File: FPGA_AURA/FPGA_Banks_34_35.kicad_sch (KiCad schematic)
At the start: 1 part, among them U1 XC7A35T-2FTG256C

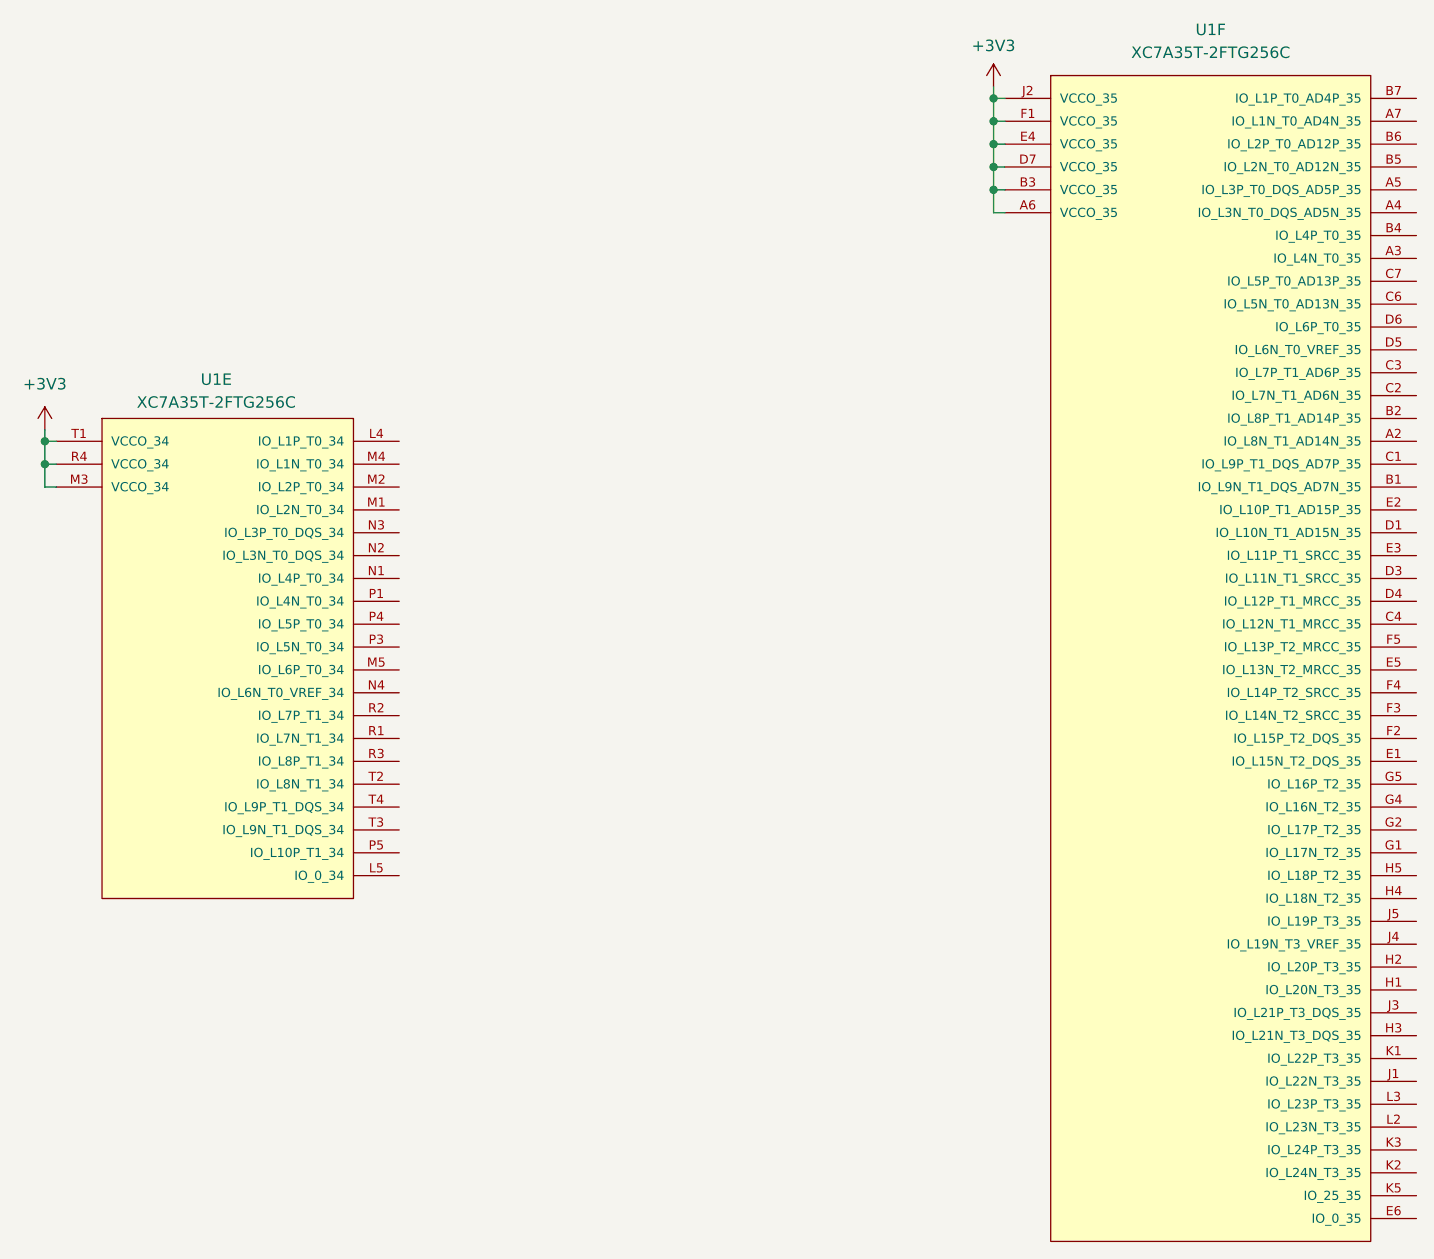
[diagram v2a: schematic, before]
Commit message: Changing stackup to 10 layers and connectors change
Development has been slow due to SI concerns with 8 layers so changing the layer count to 10 will simplify design. The picoblade/SD connector(s) are large and not high speed, so a high speed mezzanine will be used to go to a daughter board with the picoblade connectors and SD card, or other devices/protocols e.g. ADCs, COAX, IMUs, etc.
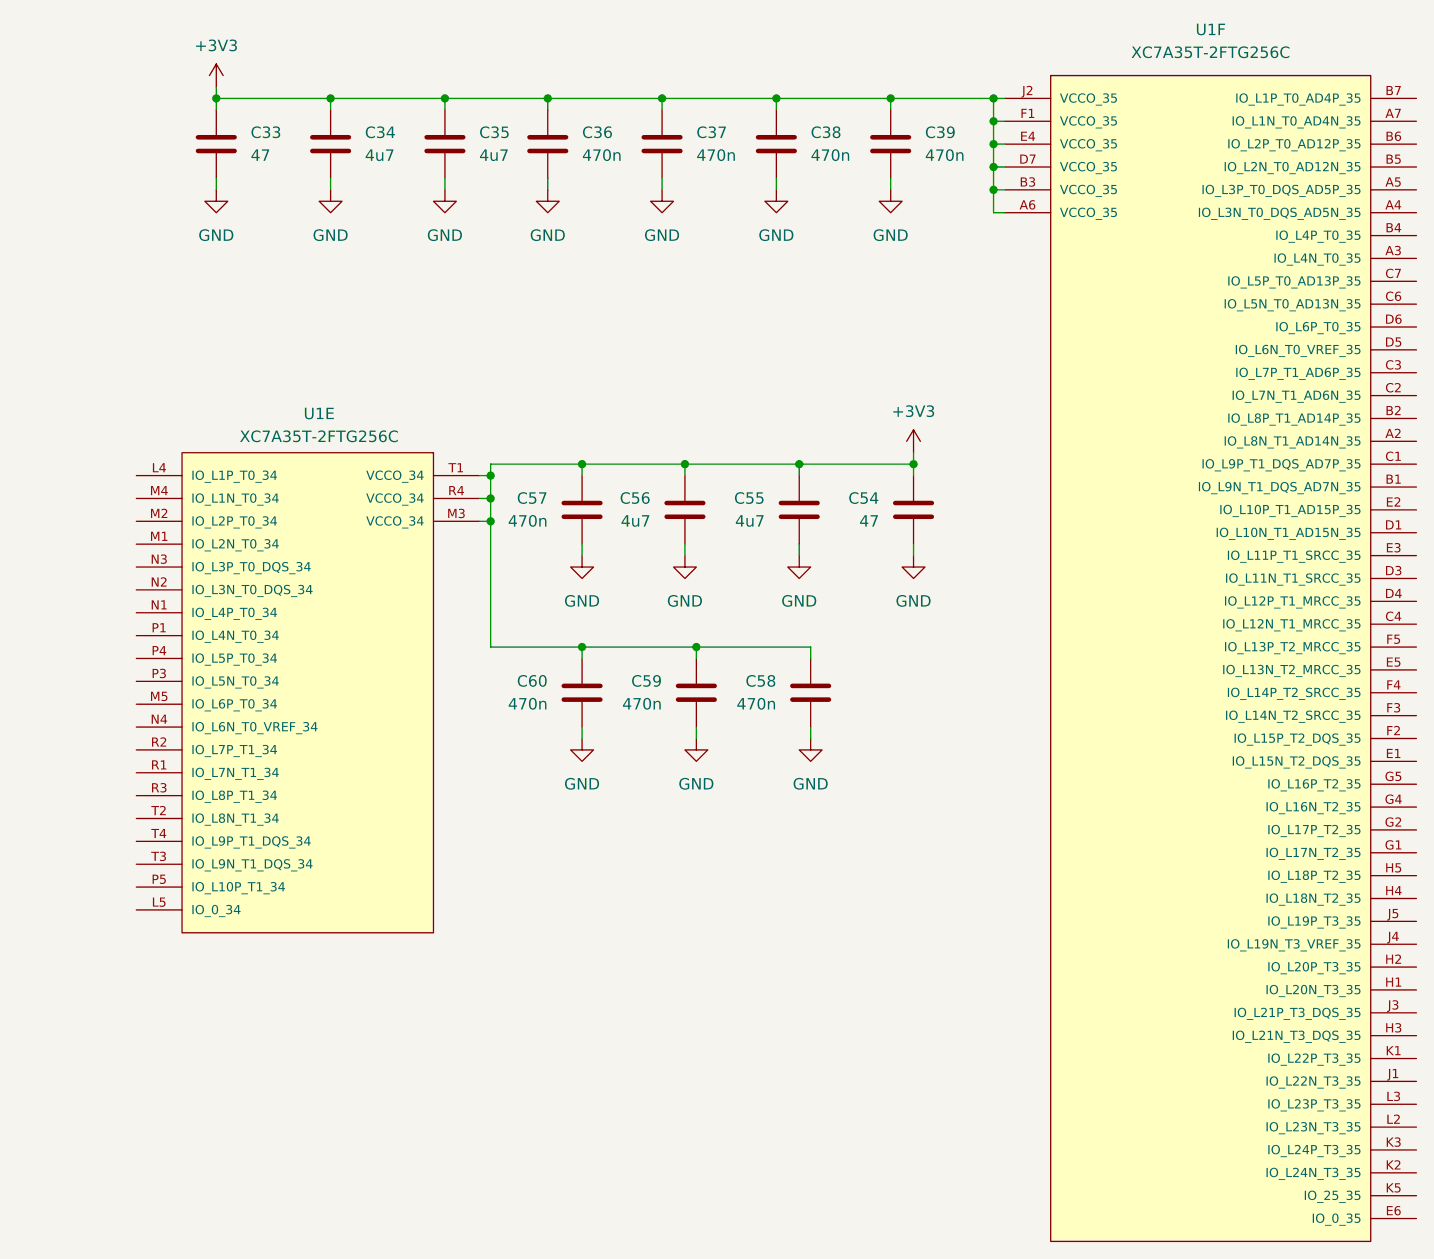
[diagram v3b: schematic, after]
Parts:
- added C33, C54: 47, Capacitor_SMD:C_0603_1608Metric, symbol Device:C
- added C34, C35, C55, C56: 4u7, Capacitor_SMD:C_0603_1608Metric, symbol Device:C
- added C36, C37, C38, C39, C57, C58, C59, C60: 470n, Capacitor_SMD:C_0402_1005Metric, symbol Device:C
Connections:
- net +3V3: now also C33.1, C34.1, C35.1, C36.1, C37.1, C38.1, C39.1, C54.1, C55.1, C56.1, C57.1, C58.1, C59.1, C60.1
- new net GND: C33.2, C34.2, C35.2, C36.2, C37.2, C38.2, C39.2, C54.2, C55.2, C56.2, C57.2, C58.2, C59.2, C60.2
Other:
- moved on the sheet: U1E
